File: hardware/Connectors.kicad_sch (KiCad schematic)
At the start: 19 parts, among them J1 Conn_02x04_Counter_Clockwise, J2 Conn_02x05_Odd_Even, Q1 DMN65D8L-7, Q2 DMN65D8L-7, U2 FXL4TD245BQX

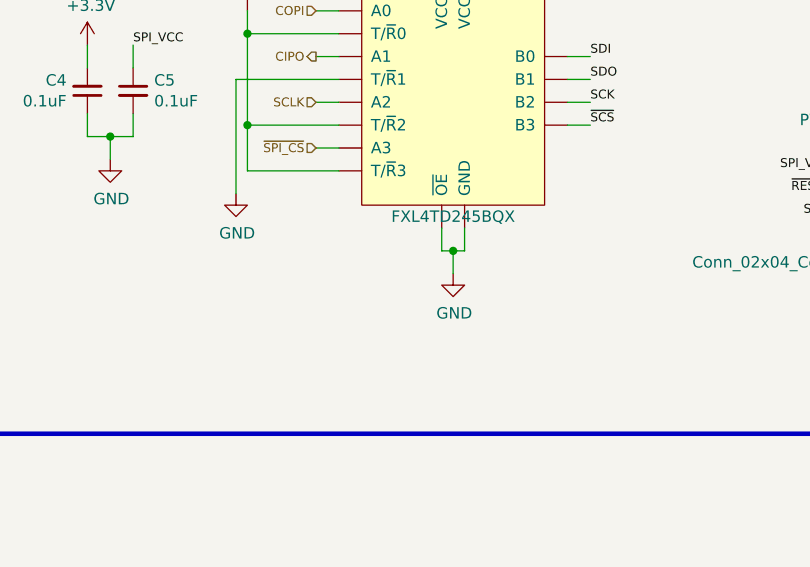
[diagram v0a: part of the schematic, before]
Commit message: Added control for the level shifter output enable to the CPU to fix problems caused by us accidentally still driving the external bus after reset is released
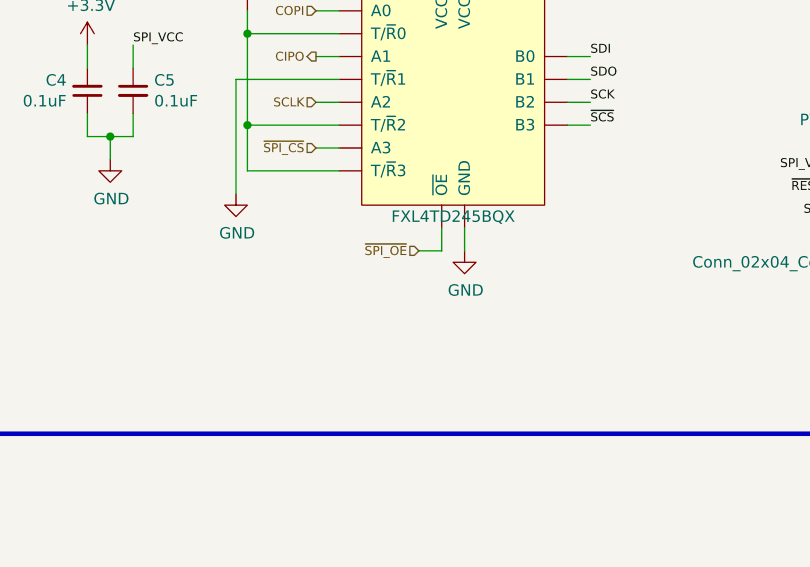
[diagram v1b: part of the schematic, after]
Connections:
- net GND: no longer U2.9 (~{OE})
- new net ~{SPI_OE}: U2.9 (~{OE})
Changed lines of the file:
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@@
   (junction (at 49.53 157.48) (diameter 0) (color 0 0 0 0)
-  )
-  (junction (at 190.5 81.28) (diameter 0) (color 0 0 0 0)
   )
   (no_connect (at 69.85 66.04))
@@
     (stroke (width 0) (type default) (color 0 0 0 0))
   )
-  (wire (pts (xy 189.23 81.28) (xy 190.5 81.28))
-    (stroke (width 0) (type default) (color 0 0 0 0))
-  )
-  (wire (pts (xy 191.77 81.28) (xy 190.5 81.28))
-    (stroke (width 0) (type default) (color 0 0 0 0))
-  )
   (wire (pts (xy 177.8 69.85) (xy 175.26 69.85))
     (stroke (width 0) (type default) (color 0 0 0 0))
@@
     (stroke (width 0.508) (type solid) (color 204 0 0 1))
   )
-  (wire (pts (xy 190.5 81.28) (xy 190.5 83.82))
-    (stroke (width 0) (type default) (color 0 0 0 0))
-  )
   (wire (pts (xy 72.39 58.42) (xy 72.39 55.88))
     (stroke (width 0) (type default) (color 0 0 0 0))
@@
     (stroke (width 0) (type default) (color 0 0 0 0))
   )
+  (wire (pts (xy 186.69 81.28) (xy 189.23 81.28))
+    (stroke (width 0) (type default) (color 0 0 0 0))
+  )
   (text "JTAG" (at 13.97 17.78 0)
     (effects (font (size 3.9878 3.9878)) (justify left bottom))
@@
   (hierarchical_label "~{SRST}" (shape output) (at 54.61 68.58 180)
     (effects (font (size 0.9906 0.9906)) (justify right))
+  )
+  (hierarchical_label "~{SPI_OE}" (shape input) (at 186.69 81.28 180)
+    (effects (font (size 1 1)) (justify right))
   )
   (hierarchical_label "~{SPI_PRESENT}" (shape output) (at 154.94 147.32 0)
@@
     (pin "1")
   )
-  (symbol (lib_id "power:GND") (at 190.5 83.82 0) (unit 1)
-    (in_bom yes) (on_board yes)
-    (property "Reference" "#PWR010" (id 0) (at 190.5 90.17 0)
-      (effects (font (size 1.27 1.27)) hide)
-    )
-    (property "Value" "GND" (id 1) (at 190.627 88.2142 0))
-    (property "Footprint" "" (id 2) (at 190.5 83.82 0)
-      (effects (font (size 1.27 1.27)) hide)
-    )
-    (property "Datasheet" "" (id 3) (at 190.5 83.82 0)
+  (symbol (lib_id "power:GND") (at 191.77 81.28 0) (unit 1)
+    (in_bom yes) (on_board yes)
+    (property "Reference" "#PWR010" (id 0) (at 191.77 87.63 0)
+      (effects (font (size 1.27 1.27)) hide)
+    )
+    (property "Value" "GND" (id 1) (at 191.897 85.6742 0))
+    (property "Footprint" "" (id 2) (at 191.77 81.28 0)
+      (effects (font (size 1.27 1.27)) hide)
+    )
+    (property "Datasheet" "" (id 3) (at 191.77 81.28 0)
       (effects (font (size 1.27 1.27)) hide)
     )
@@
     )
   )
-  (symbol (lib_id "Device:R_Small") (at 152.4 142.24 0)
+  (symbol (lib_id "Device:R_Small") (at 152.4 142.24 0) (unit 1)
     (in_bom yes) (on_board yes)
     (property "Reference" "R12" (id 0) (at 153.8986 141.0716 0)
@@
     (pin "2")
   )
-  (symbol (lib_id "Device:LED") (at 152.4 130.81 90)
+  (symbol (lib_id "Device:LED") (at 152.4 130.81 90) (unit 1)
     (in_bom yes) (on_board yes)
     (property "Reference" "D2" (id 0) (at 155.3972 129.8194 90)
@@
     (pin "2")
   )
-  (symbol (lib_id "power:+3.3V") (at 152.4 124.46 0)
+  (symbol (lib_id "power:+3.3V") (at 152.4 124.46 0) (unit 1)
     (in_bom yes) (on_board yes)
     (property "Reference" "#PWR038" (id 0) (at 152.4 128.27 0)
@@
     (pin "1")
   )
-  (symbol (lib_id "power:GND") (at 152.4 162.56 0)
+  (symbol (lib_id "power:GND") (at 152.4 162.56 0) (unit 1)
     (in_bom yes) (on_board yes)
     (property "Reference" "#PWR039" (id 0) (at 152.4 168.91 0)
@@
     )
   )
-  (symbol (lib_id "Device:R_Small") (at 165.1 154.94 270)
+  (symbol (lib_id "Device:R_Small") (at 165.1 154.94 270) (unit 1)
     (in_bom yes) (on_board yes)
     (property "Reference" "R13" (id 0) (at 165.1 149.9616 90))
